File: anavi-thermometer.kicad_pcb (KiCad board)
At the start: 2 copper layers, 74.9 x 40.6 mm, 25 parts, among them P1 CONN_01X03, U1 I2C_SENS_1, U2 I2C_SENS_1, U3 I2C_SENS_1

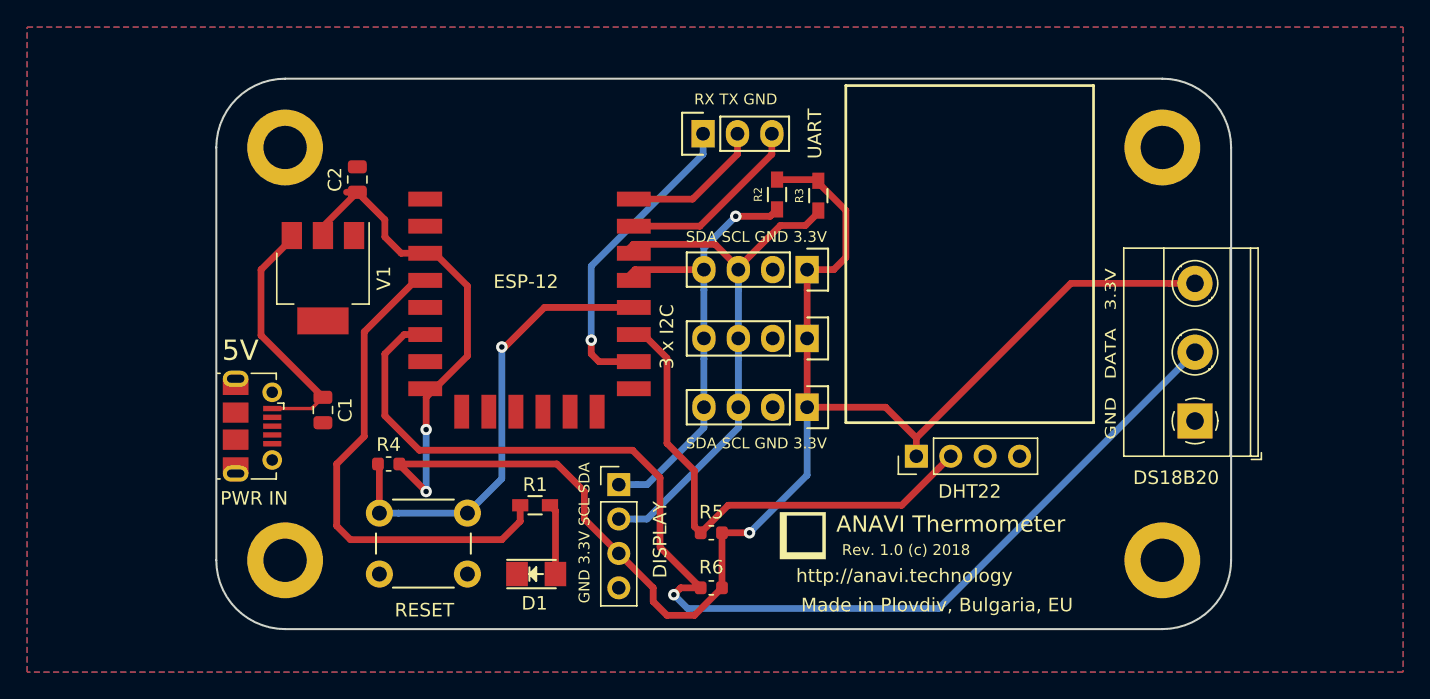
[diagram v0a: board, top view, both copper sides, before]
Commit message: anavi-thermometer.kicad_pcb: Update silkscreen
Move the contour of DHT22 to the fab layer.

Signed-off-by: Leon Anavi <leon@anavi.org>
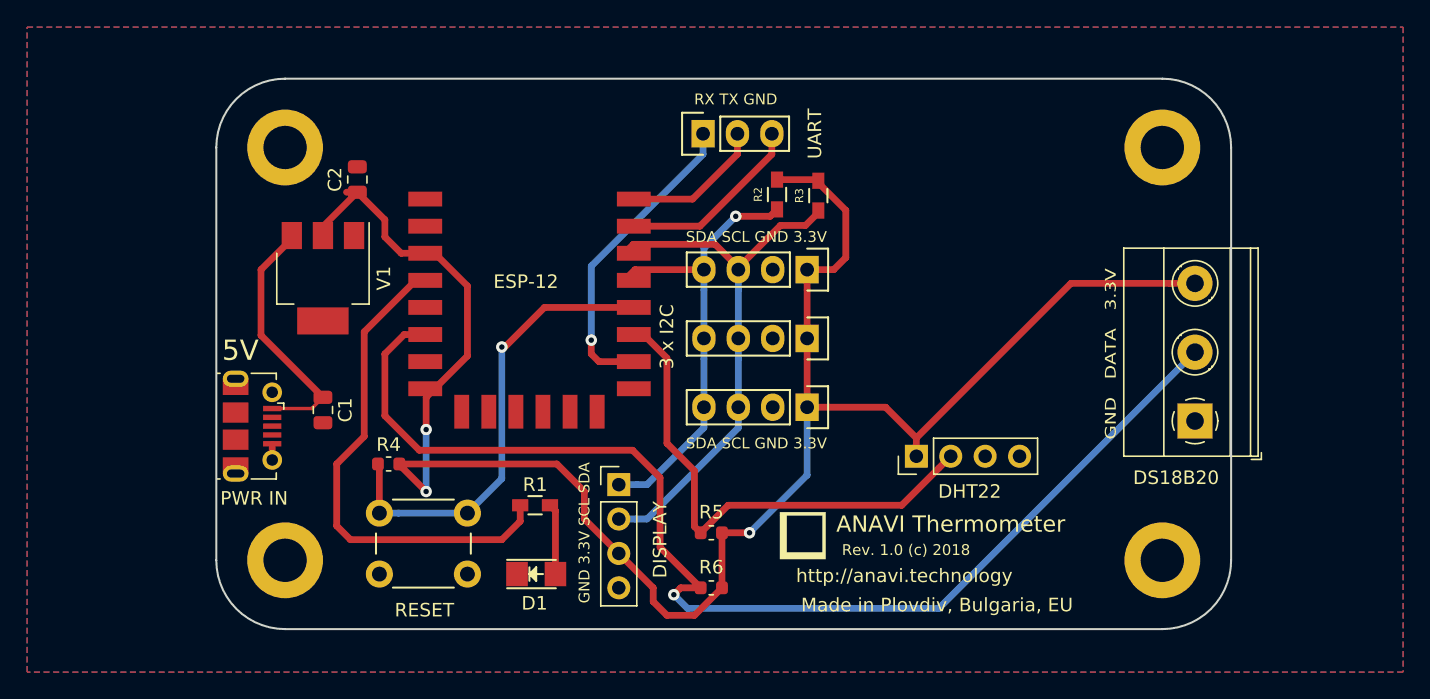
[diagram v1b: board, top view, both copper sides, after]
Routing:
- net GND: track 22.4 -> 23.5 mm
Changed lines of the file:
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@@
     (thickness 1.6)
     (drawings 25)
-    (tracks 150)
+    (tracks 151)
     (zones 0)
     (modules 25)
@@
   )
   (setup
-    (last_trace_width 0.5)
+    (last_trace_width 0.254)
     (user_trace_width 0.254)
     (user_trace_width 0.5)
@@
     )
   )
+  (gr_line (start 111.252 96.52) (end 111.252 71.628) (layer F.Fab) (width 0.2))
+  (gr_line (start 129.54 71.628) (end 111.252 71.628) (layer F.Fab) (width 0.2))
+  (gr_line (start 129.54 96.52) (end 129.54 71.628) (layer F.Fab) (width 0.2))
+  (gr_line (start 111.252 96.52) (end 129.54 96.52) (layer F.Fab) (width 0.2))
   (gr_text "GND   DATA   3.3V" (at 130.81 91.44 90) (layer F.SilkS)
     (effects (font (size 0.8 1) (thickness 0.15)))
@@
     (effects (font (size 0.8 0.8) (thickness 0.15)))
   )
-  (gr_line (start 111.252 71.628) (end 111.252 96.52) (layer F.SilkS) (width 0.2))
-  (gr_line (start 129.54 71.628) (end 111.252 71.628) (layer F.SilkS) (width 0.2))
-  (gr_line (start 129.54 96.52) (end 129.54 71.628) (layer F.SilkS) (width 0.2))
-  (gr_line (start 111.252 96.52) (end 129.54 96.52) (layer F.SilkS) (width 0.2))
   (gr_text KP-3216EC (at 88.392 109.728) (layer F.Fab)
     (effects (font (size 0.8 0.8) (thickness 0.15)))
@@
   (segment (start 93.026 92.01) (end 94.899 92.01) (width 0.5) (layer F.Cu) (net 2))
   (segment (start 92.456 91.44) (end 93.026 92.01) (width 0.5) (layer F.Cu) (net 2))
+  (segment (start 68.8995 99.274) (end 68.8995 98.128001) (width 0.5) (layer F.Cu) (net 2))
   (segment (start 108.288 85.1105) (end 108.3945 85.217) (width 0.5) (layer F.Cu) (net 3))
   (segment (start 74.384 79.502) (end 75.184 79.502) (width 0.5) (layer F.Cu) (net 3))
